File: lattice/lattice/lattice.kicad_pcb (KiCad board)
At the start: 2 copper layers, 249.1 x 128.5 mm, 143 parts, among them J1 AudioJack2, J10 AudioJack2, J11 AudioJack2, J12 AudioJack2, J13 AudioJack2, J14 AudioJack2, J15 AudioJack2, J16 Conn_02x05_Counter_Clockwise, J17 Conn_01x10, J18 Conn_01x10, J19 Conn_01x08, J2 AudioJack2, J20 Conn_01x08, J21 Conn_01x07, J22 Conn_01x07, J23 Conn_01x07, J24 Conn_01x07, J26 WEEE, J27 OSHW, J3 AudioJack2, J4 AudioJack2, J5 AudioJack2, J6 AudioJack2, J7 AudioJack2, J8 AudioJack2, J9 Conn_02x08_Odd_Even, Q1 BC548, Q2 BC548, SW1 LP4OA1PBCT, U1 MCP6002-xP, U2 MCP6002-xP, U3 MCP6002-xP, U5 6N138, U6 LM4040LP-5, U7 74HC595

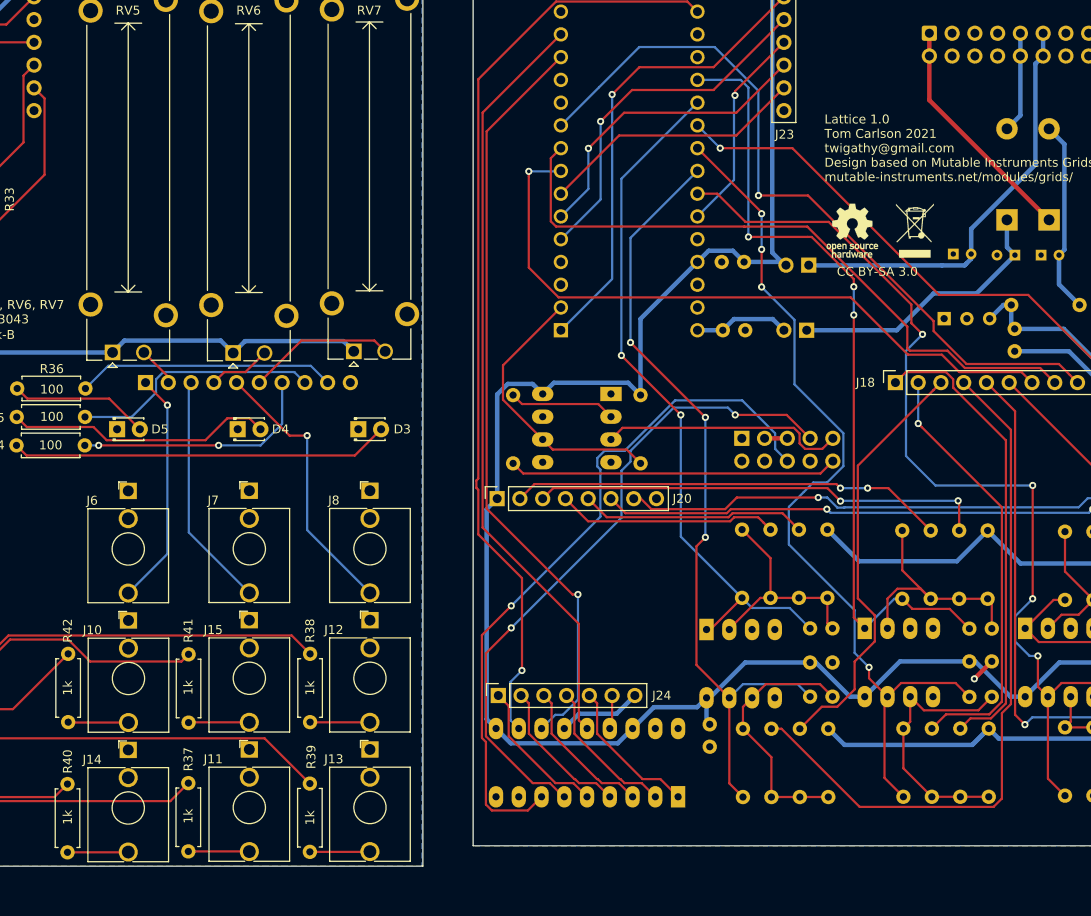
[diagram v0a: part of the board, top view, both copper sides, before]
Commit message: Fixing wrong pin assignments for triggers and accents
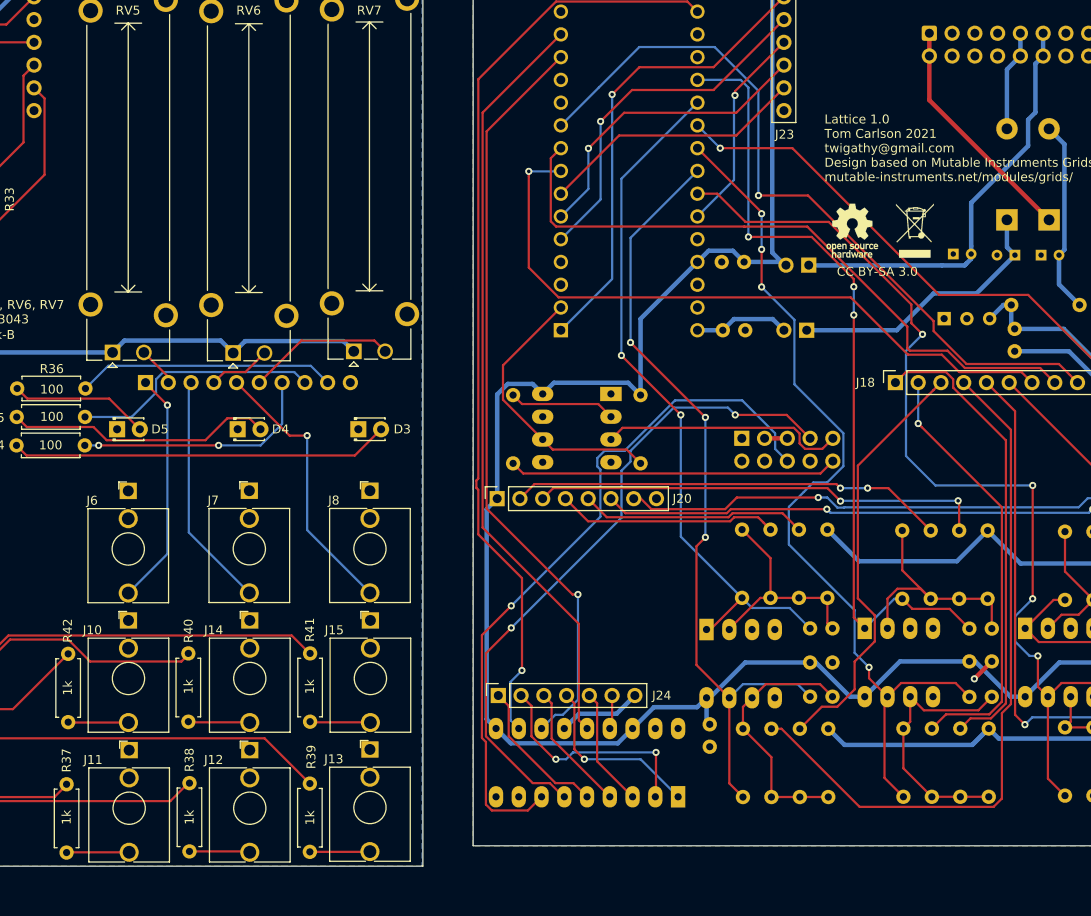
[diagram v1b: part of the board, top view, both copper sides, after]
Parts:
- moved R40 19.9 mm to (117.6, 133.7)
- moved J14 19.8 mm to (124.5, 122.4)
- moved J12 19.8 mm to (124.5, 136.9)
- moved R38 19.7 mm to (117.7, 148.2)
- moved R37 13.6 mm to (104.0, 148.3)
- moved R41 13.6 mm to (131.2, 133.7)
- moved J15 13.5 mm to (137.9, 122.4)
- moved J11 13.4 mm to (111.0, 136.9)
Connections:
- R37 pad 2: /CH2B -> /CH1B
- R38 pad 2: /CH3A -> /CH2B
- R40 pad 2: /CH1B -> /CH2A
- R41 pad 2: /CH2A -> /CH3A
- U7 pad 1: /CH1B -> /CH2A
- U7 pad 2: /CH2A -> /CH3A
- U7 pad 3: /CH2B -> /CH1B
- U7 pad 4: /CH3A -> /CH2B
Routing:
- net /CH3A: track 82.4 -> 91.1 mm, vias 1 -> 3
- net /CH2A: track 63.8 -> 67.3 mm, vias 1 -> 2
- net /CH1B: track 47.3 -> 44.1 mm
- net /CH2B: track 66.3 -> 64.1 mm

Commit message: More error-patching...
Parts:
- J16: value Conn_02x05_Counter_Clockwise -> Conn_02x05_Odd_Even
- moved J16 8.73 mm to (187.5, 105.4), turned to 90 degrees
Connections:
- J16 pad 10: /EXT_MIDI_IN_PIN_4 -> /EXT_RANDOM_GATE
- J16 pad 2: Earth -> /EXT_MIDI_IN_PIN_4
- J16 pad 4: Earth -> /EXT_MIDI_IN_PIN_5
- J16 pad 5: Earth -> +5V
- J16 pad 6: /EXT_RANDOM_GATE -> Net-(J16-Pad6)
- J16 pad 7: /EXT_RANDOM_CLOCK -> Earth
- J16 pad 8: Net-(J16-Pad8) -> /EXT_RANDOM_CLOCK
- J16 pad 9: /EXT_MIDI_IN_PIN_5 -> Earth
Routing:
- net /IN_RESET: track 56.7 -> 100.6 mm
- net +5V: track 403.0 -> 437.0 mm
- net Earth: track 30.0 -> 61.3 mm, vias 1 -> 6
- net /EXT_MIDI_IN_PIN_5: track 27.4 -> 21.4 mm
- net /EXT_RANDOM_CLOCK: track 73.5 -> 68.0 mm
- net Net-(J5-PadT): track 0.00 -> 5.06 mm
- net /EXT_RANDOM_GATE: track 79.4 -> 76.9 mm
- net /CH1_CV: track 98.5 -> 97.6 mm
- net /EXT_MIDI_IN_PIN_4: track 36.7 -> 37.5 mm

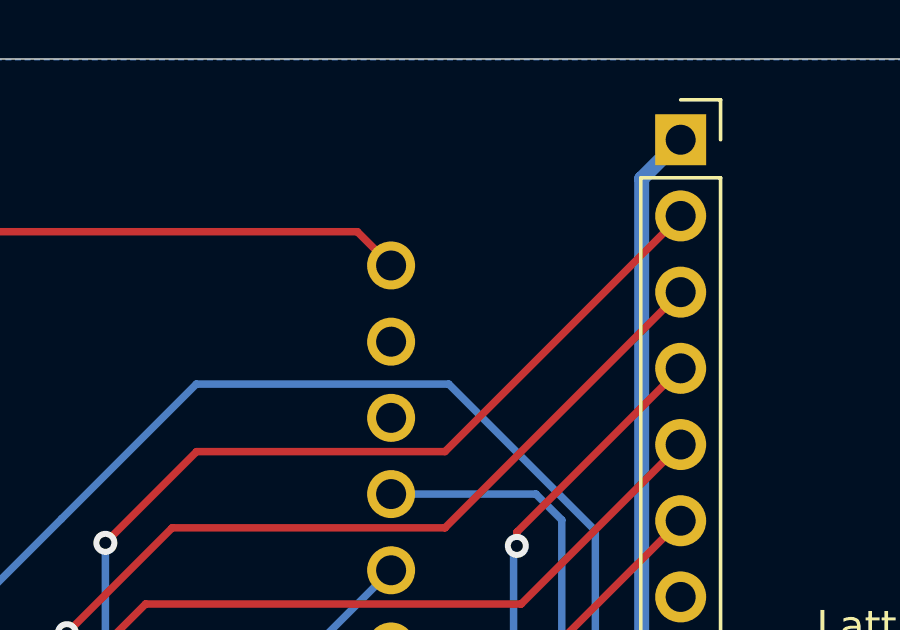
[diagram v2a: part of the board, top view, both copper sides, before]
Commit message: Adding AREF decoupling capacitor
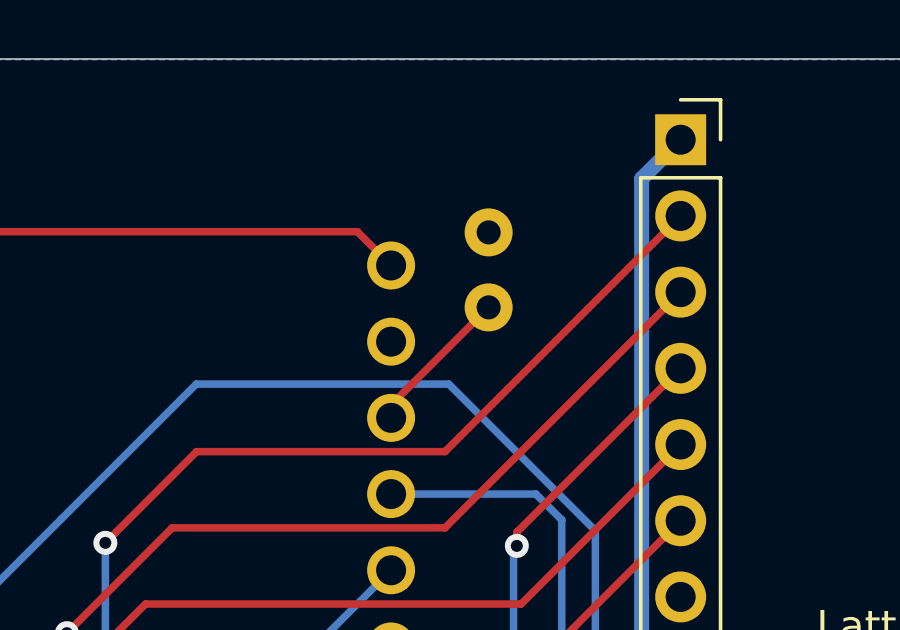
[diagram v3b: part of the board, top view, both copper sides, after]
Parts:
- added C11: 100n, Capacitor_THT:C_Disc_D3.8mm_W2.6mm_P2.50mm, B.Cu at (177.7, 55.9)
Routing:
- net Net-(A1-Pad18): track 0.00 -> 5.03 mm

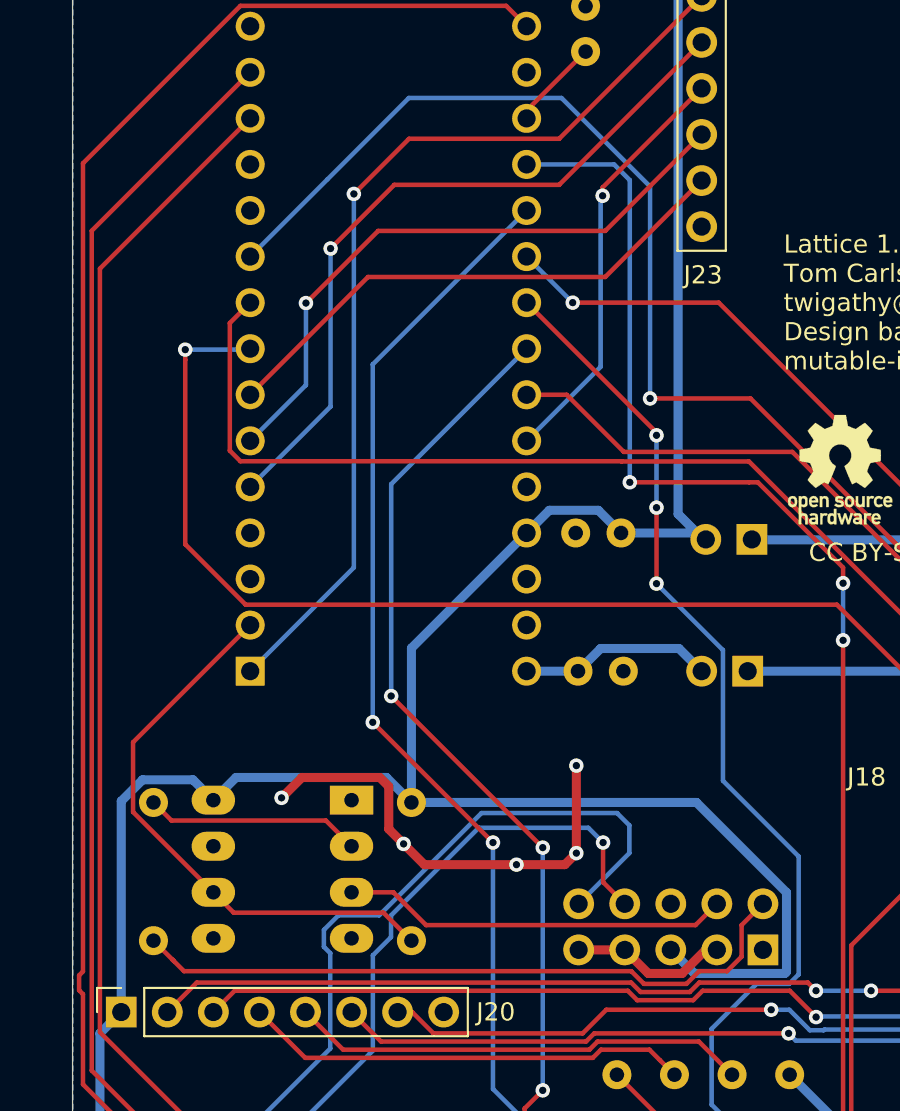
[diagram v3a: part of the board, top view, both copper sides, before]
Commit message: Adding expansion ports from the Arduino
Not used in the default firmware, but if someone comes up with something neat....
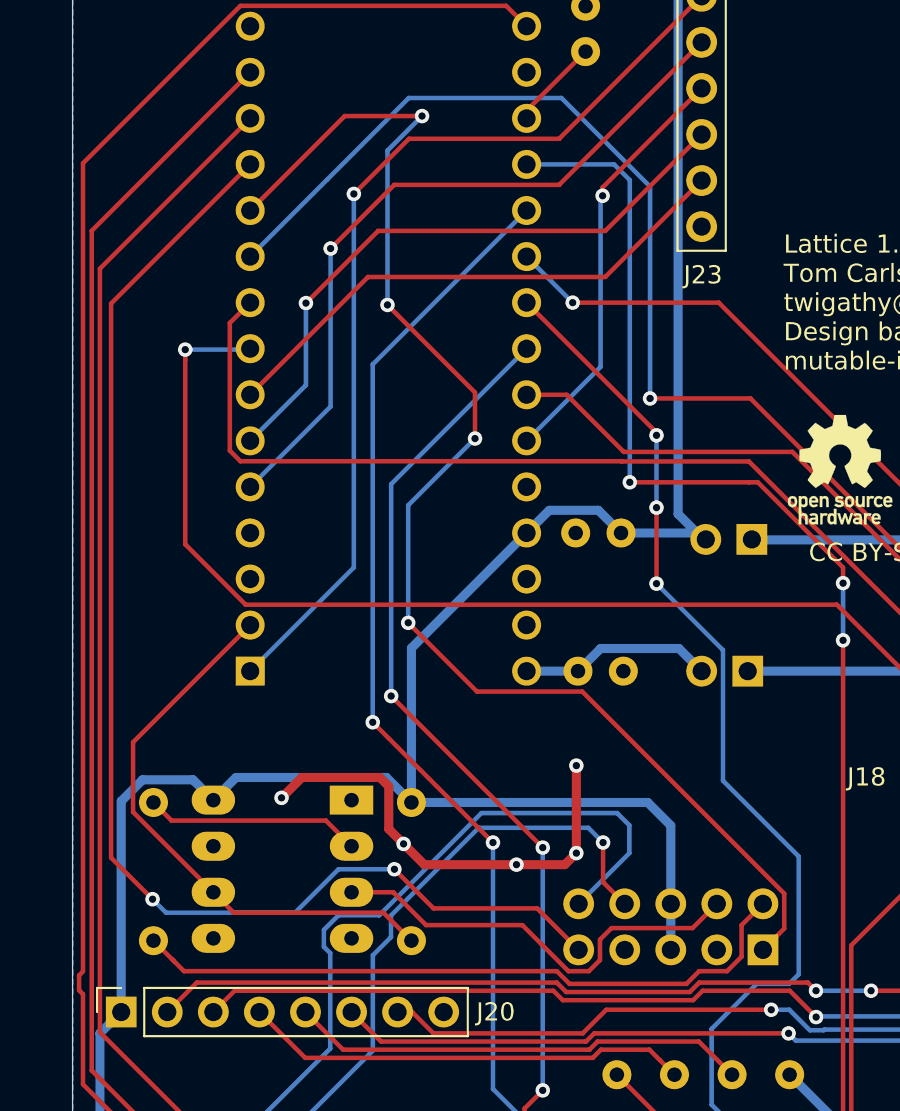
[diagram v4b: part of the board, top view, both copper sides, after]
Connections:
- A1 pad 11: Net-(A1-Pad11) -> /EXPANSION_1
- A1 pad 12: Net-(A1-Pad12) -> /EXPANSION_2
- J16 pad 1: Earth -> /EXPANSION_1
- J16 pad 6: Net-(J16-Pad6) -> +5V
- J16 pad 9: Earth -> /EXPANSION_2
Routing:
- net /EXPANSION_1: track 0.00 -> 74.4 mm, vias 0 -> 4
- net /EXPANSION_2: track 0.00 -> 71.3 mm, vias 0 -> 2
- net +5V: track 437.0 -> 424.6 mm
- net Earth: track 61.3 -> 52.6 mm
- net /EXT_MIDI_IN_PIN_5: track 21.4 -> 24.1 mm

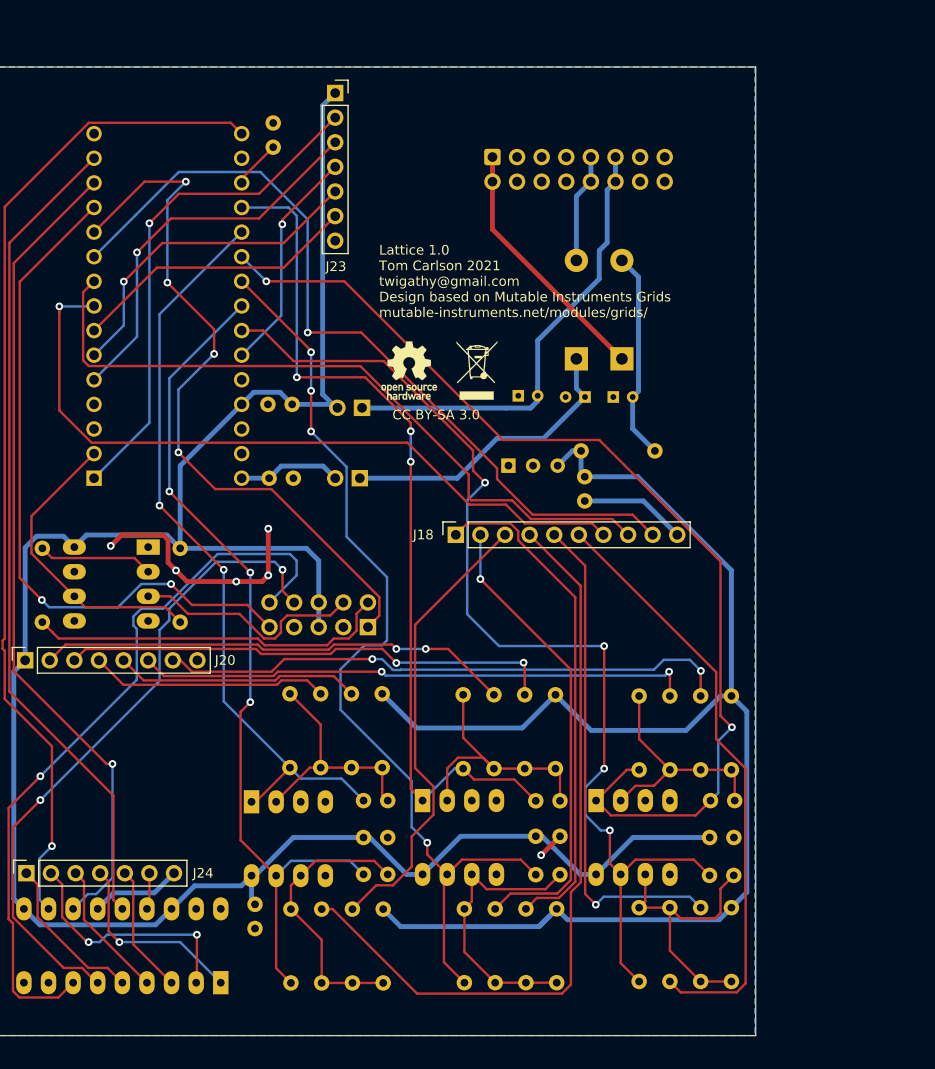
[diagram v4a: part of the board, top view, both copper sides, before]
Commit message: Adding expansion board
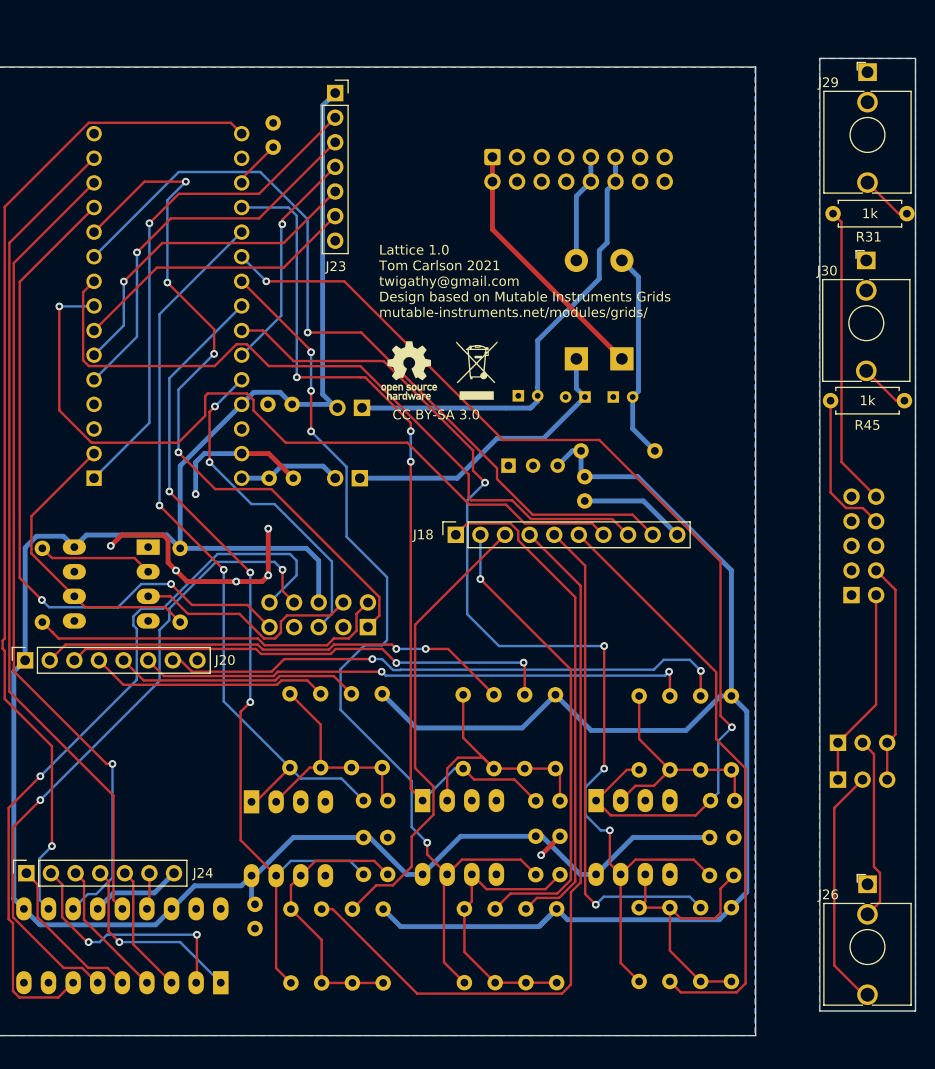
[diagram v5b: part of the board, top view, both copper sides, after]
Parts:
- added J25: Conn_02x05_Odd_Even, Connector_PinHeader_2.54mm:PinHeader_2x05_P2.54mm_Vertical, B.Cu at (237.4, 102.1)
- added J26: AudioJack3, RS:Jack_3.5mm_QingPu_WQP-PJ398SM_Vertical_CircularHoles, F.Cu at (239.0, 132.0)
- added J27: Conn_01x03, Connector_PinHeader_2.54mm:PinHeader_1x03_P2.54mm_Vertical, B.Cu at (236.0, 117.3)
- added J28: Conn_01x03, Connector_PinHeader_2.54mm:PinHeader_1x03_P2.54mm_Vertical, B.Cu at (236.0, 121.2)
- added J29: AudioJack2, Connector_Audio:Jack_3.5mm_QingPu_WQP-PJ398SM_Vertical_CircularHoles, F.Cu at (239.0, 48.1)
- added J30: AudioJack2, Connector_Audio:Jack_3.5mm_QingPu_WQP-PJ398SM_Vertical_CircularHoles, F.Cu at (238.9, 67.6)
- added R31: 1k, Resistor_THT:R_Axial_DIN0207_L6.3mm_D2.5mm_P7.62mm_Horizontal, F.Cu at (235.5, 62.7)
- added R45: 1k, Resistor_THT:R_Axial_DIN0207_L6.3mm_D2.5mm_P7.62mm_Horizontal, F.Cu at (235.2, 82.0)
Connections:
- A1 pad 26: Net-(A1-Pad26) -> /EXPANSION_3
- J16 pad 5: +5V -> /EXPANSION_3
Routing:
- net /EXPANSION_3: track 0.00 -> 34.1 mm, vias 0 -> 2
- net /EXT_RANDOM_GATE: track 76.9 -> 108.0 mm
- net /MIDI_TIP: track 0.00 -> 25.1 mm
- net /EXT_MIDI_IN_PIN_5: track 24.1 -> 46.9 mm
- net /EXT_MIDI_IN_PIN_4: track 37.5 -> 58.2 mm
- net /MIDI_RING: track 0.00 -> 19.0 mm
- net /EXT_RANDOM_CLOCK: track 68.0 -> 83.4 mm
- net Earth: track 52.6 -> 67.4 mm, vias 6 -> 7
- net /LED_CH3: track 103.5 -> 109.5 mm
- net Net-(J29-PadT): track 0.00 -> 5.39 mm
- net Net-(J30-PadT): track 0.00 -> 5.21 mm
- net +5V: track 424.6 -> 422.1 mm
- net /LED_CH2: track 101.7 -> 103.6 mm
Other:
- board size 249.1 x 128.5 mm -> 265.6 x 128.5 mm
- board text added: "A"
- board text added: "B"
- board text added: "Ring"
- board text added: "Tip"

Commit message: Fiddling with silkscreen
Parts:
- added J26: WEEE, Symbol:WEEE-Logo_4.2x6mm_SilkScreen, B.Cu at (239.3, 88.3)
- added J26: WEEE, Symbol:WEEE-Logo_4.2x6mm_SilkScreen, B.Cu at (260.1, 46.7)
- added J27: OSHW, Symbol:OSHW-Logo_5.7x6mm_SilkScreen, B.Cu at (237.2, 140.0)
- added J27: OSHW, Symbol:OSHW-Logo_5.7x6mm_SilkScreen, B.Cu at (260.1, 65.0)
- added REF**: MountingHole_3.2mm_M3, MountingHole:MountingHole_3.2mm_M3, F.Cu at (260.4, 139.2)
- added REF**: MountingHole_3.2mm_M3, MountingHole:MountingHole_3.2mm_M3, F.Cu at (260.2, 74.8)
- added REF**: MountingHole_3.2mm_M3, MountingHole:MountingHole_3.2mm_M3, F.Cu at (260.4, 55.4)
- added REF**: MountingHole_3.2mm_M3, MountingHole:MountingHole_3.2mm_M3, F.Cu at (258.4, 37.4)
- added REF**: MountingHole_3.2mm_M3, MountingHole:MountingHole_3.2mm_M3, F.Cu at (258.3, 159.8)
- R31, R45: moved to B.Cu
- moved R31 1.05 mm to (235.2, 63.8)
- moved J25 0.76 mm to (237.4, 102.9)
- moved J26 0.76 mm to (239.0, 132.7)
- moved J27 0.76 mm to (236.0, 118.1)
- moved J28 0.76 mm to (236.0, 121.9)
- moved J29 0.76 mm to (239.0, 48.9)
- moved J30 0.76 mm to (238.9, 68.3)
- moved R45 0.76 mm to (235.2, 82.8)
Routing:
- added copper zone on F.Cu, net Earth
- removed copper zone on F.Cu, net (none)
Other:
- board size 265.6 x 128.5 mm -> 286.9 x 128.7 mm
- board text added: "Clocks"
- board text added: "Gates"
- board text added: "MIDI In"
- board text added: "Mesh"
- board text added: "Mesh 1.0 Tom Carlson 2021 twigathy@gmail.com"
